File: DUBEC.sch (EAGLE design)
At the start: 69 parts

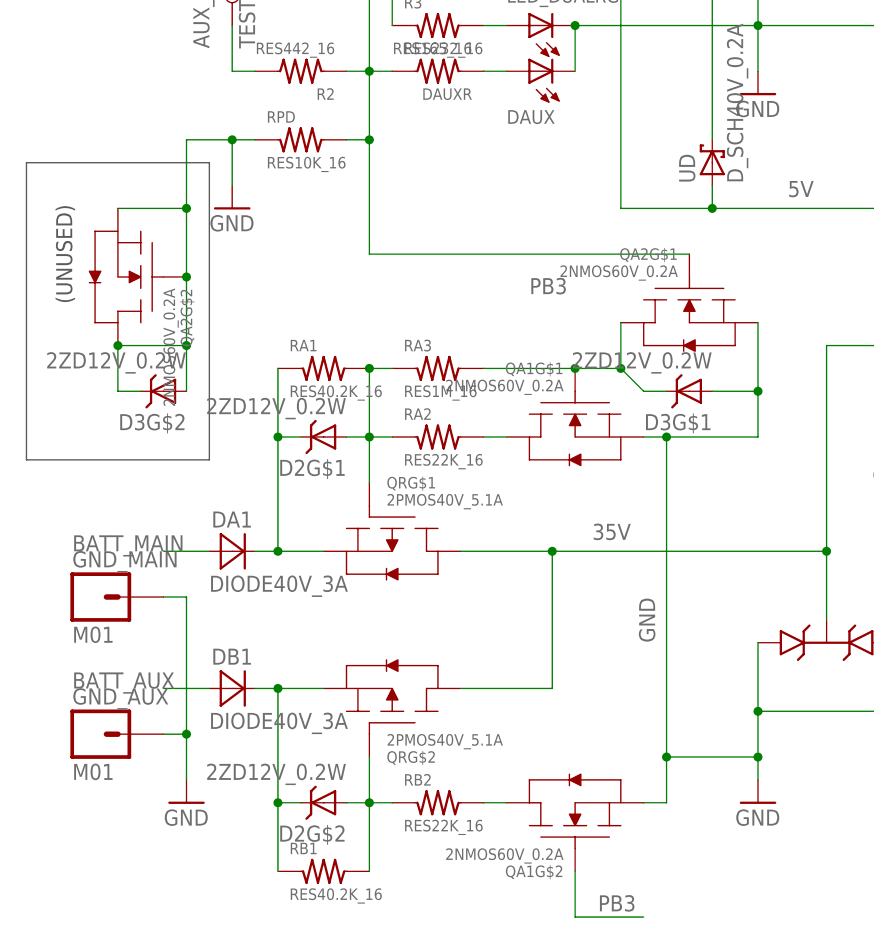
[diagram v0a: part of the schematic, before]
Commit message: Fixed one schematic error
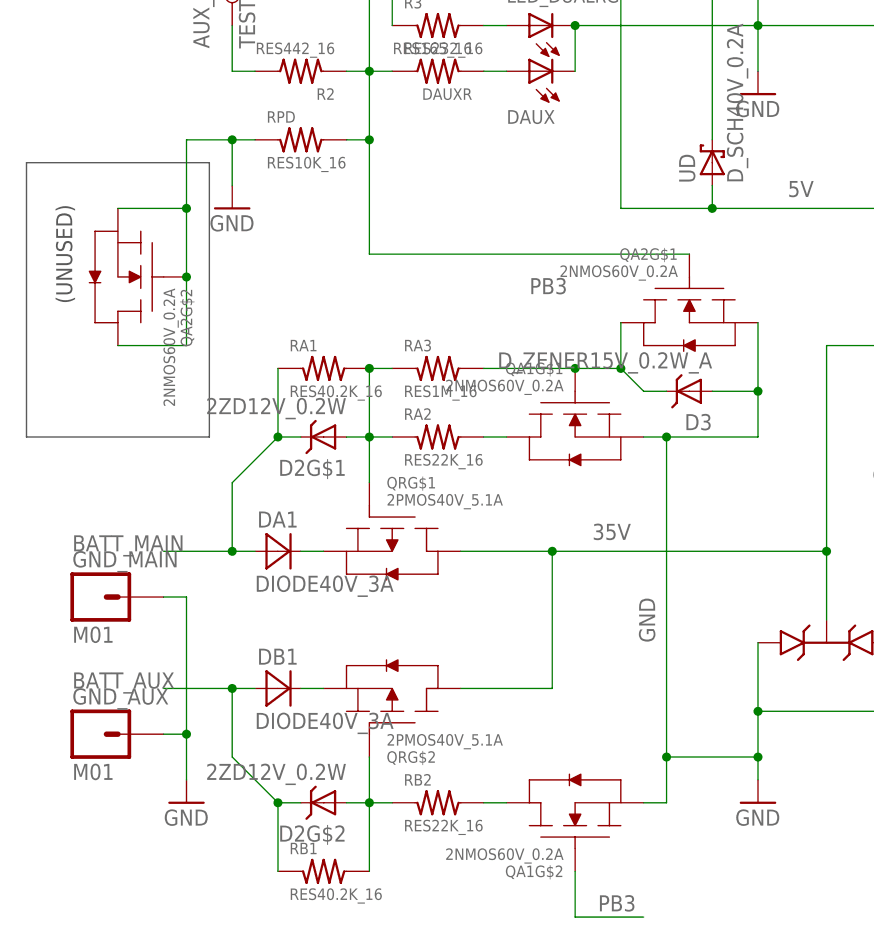
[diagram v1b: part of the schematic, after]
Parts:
- D3: value 2ZD12V_0.2W -> D_ZENER15V_0.2W_A; device dubec:2ZD12V_0.2W -> dubec:D_ZENER15V_0.2W_A
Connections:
- removed net V_AUX: D2G$2.C, DB1.C, QRG$2.S, RB1.1
- removed net V_MAIN: D2G$1.C, DA1.C, QRG$1.S, RA1.1
- new net N$6: DA1.C, QRG$1.S
- new net N$8: DB1.C, QRG$2.S
- net BATT_AUX: now also D2G$2.C, RB1.1
- net BATT_MAIN: now also D2G$1.C, RA1.1
- net GATE_MAIN_B: now also D3.C; no longer D3G$1.C
- net GND: now also D3.A; no longer D3G$1.A, D3G$2.A, D3G$2.C
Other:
- moved on the sheet: DA1, DB1
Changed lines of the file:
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@@
 <setting verticaltext="up"/>
 </settings>
-<grid distance="0.1" unitdist="inch" unit="inch" style="lines" multiple="1" display="no" altdistance="0.025" altunitdist="inch" altunit="inch"/>
+<grid distance="0.1" unitdist="inch" unit="inch" style="lines" multiple="1" display="no" altdistance="0.01" altunitdist="inch" altunit="inch"/>
 <layers>
 <layer number="1" name="Top" color="4" fill="1" visible="no" active="no"/>
@@
 <part name="RA3" library="dubec" deviceset="RES" device="1M_16" value="RES1M_16"/>
 <part name="QA2" library="dubec" deviceset="2NMOS" device="60V_0.2A"/>
-<part name="D3" library="dubec" deviceset="2ZD" device="12V_0.2W"/>
+<part name="D3" library="dubec" deviceset="D_ZENER" device="15V_0.2W_A"/>
 </parts>
 <sheets>
@@
 <text x="-129.54" y="-12.7" size="1.778" layer="97" rot="R90" align="bottom-center">(UNUSED)</text>
 <wire x1="-134.62" y1="-2.54" x2="-114.3" y2="-2.54" width="0.1524" layer="97"/>
-<wire x1="-114.3" y1="-2.54" x2="-114.3" y2="-35.56" width="0.1524" layer="97"/>
-<wire x1="-114.3" y1="-35.56" x2="-134.62" y2="-35.56" width="0.1524" layer="97"/>
-<wire x1="-134.62" y1="-35.56" x2="-134.62" y2="-2.54" width="0.1524" layer="97"/>
+<wire x1="-114.3" y1="-2.54" x2="-114.3" y2="-33.02" width="0.1524" layer="97"/>
+<wire x1="-114.3" y1="-33.02" x2="-134.62" y2="-33.02" width="0.1524" layer="97"/>
+<wire x1="-134.62" y1="-33.02" x2="-134.62" y2="-2.54" width="0.1524" layer="97"/>
 </plain>
 <instances>
@@
 <instance part="QA1" gate="G$2" x="-73.66" y="-73.66" rot="R90"/>
 <instance part="GND6" gate="1" x="-53.34" y="-73.66"/>
-<instance part="DA1" gate="G$1" x="-111.76" y="-45.72"/>
-<instance part="DB1" gate="G$1" x="-111.76" y="-60.96"/>
+<instance part="DA1" gate="G$1" x="-106.68" y="-45.72"/>
+<instance part="DB1" gate="G$1" x="-106.68" y="-60.96"/>
 <instance part="GND_MAIN" gate="G$1" x="-124.46" y="-50.8"/>
 <instance part="GND_AUX" gate="G$1" x="-124.46" y="-66.04"/>
@@
 <instance part="QA2" gate="G$2" x="-124.46" y="-15.24" rot="R180"/>
 <instance part="D3" gate="G$1" x="-60.96" y="-27.94" rot="R180"/>
-<instance part="D3" gate="G$2" x="-119.38" y="-27.94" rot="R180"/>
 </instances>
 <busses>
@@
 <wire x1="-124.46" y1="-7.62" x2="-116.84" y2="-7.62" width="0.1524" layer="91"/>
 <junction x="-116.84" y="-7.62"/>
-<pinref part="D3" gate="G$2" pin="A"/>
-<wire x1="-116.84" y1="-22.86" x2="-116.84" y2="-27.94" width="0.1524" layer="91"/>
-<junction x="-116.84" y="-22.86"/>
-<pinref part="D3" gate="G$2" pin="C"/>
-<wire x1="-121.92" y1="-27.94" x2="-124.46" y2="-27.94" width="0.1524" layer="91"/>
-<wire x1="-124.46" y1="-27.94" x2="-124.46" y2="-22.86" width="0.1524" layer="91"/>
-<junction x="-124.46" y="-22.86"/>
 </segment>
 <segment>
@@
 <wire x1="-58.42" y1="-27.94" x2="-53.34" y2="-27.94" width="0.1524" layer="91"/>
 <junction x="-53.34" y="-27.94"/>
+<label x="-64.77" y="-55.88" size="1.778" layer="95" rot="R90"/>
 <pinref part="D3" gate="G$1" pin="A"/>
-<label x="-64.77" y="-55.88" size="1.778" layer="95" rot="R90"/>
 </segment>
 </net>
@@
 <segment>
 <pinref part="DA1" gate="G$1" pin="A"/>
-<wire x1="-119.38" y1="-45.72" x2="-114.3" y2="-45.72" width="0.1524" layer="91"/>
+<wire x1="-119.38" y1="-45.72" x2="-111.76" y2="-45.72" width="0.1524" layer="91"/>
 <label x="-129.54" y="-45.72" size="1.778" layer="95"/>
-</segment>
-</net>
-<net name="V_MAIN" class="2">
-<segment>
-<pinref part="DA1" gate="G$1" pin="C"/>
-<pinref part="QR" gate="G$1" pin="S"/>
-<wire x1="-109.22" y1="-45.72" x2="-106.68" y2="-45.72" width="0.1524" layer="91"/>
+<wire x1="-111.76" y1="-45.72" x2="-109.22" y2="-45.72" width="0.1524" layer="91"/>
+<wire x1="-111.76" y1="-45.72" x2="-111.76" y2="-38.1" width="0.1524" layer="91"/>
+<junction x="-111.76" y="-45.72"/>
+<wire x1="-111.76" y1="-38.1" x2="-106.68" y2="-33.02" width="0.1524" layer="91"/>
 <pinref part="D2" gate="G$1" pin="C"/>
-<wire x1="-106.68" y1="-45.72" x2="-101.6" y2="-45.72" width="0.1524" layer="91"/>
-<wire x1="-104.14" y1="-33.02" x2="-106.68" y2="-33.02" width="0.1524" layer="91"/>
-<wire x1="-106.68" y1="-33.02" x2="-106.68" y2="-45.72" width="0.1524" layer="91"/>
-<junction x="-106.68" y="-45.72"/>
+<wire x1="-106.68" y1="-33.02" x2="-104.14" y2="-33.02" width="0.1524" layer="91"/>
 <pinref part="RA1" gate="G$1" pin="1"/>
 <wire x1="-106.68" y1="-25.4" x2="-106.68" y2="-33.02" width="0.1524" layer="91"/>
@@
 <segment>
 <pinref part="DB1" gate="G$1" pin="A"/>
-<wire x1="-119.38" y1="-60.96" x2="-114.3" y2="-60.96" width="0.1524" layer="91"/>
+<wire x1="-119.38" y1="-60.96" x2="-111.76" y2="-60.96" width="0.1524" layer="91"/>
 <label x="-129.54" y="-60.96" size="1.778" layer="95"/>
+<wire x1="-111.76" y1="-60.96" x2="-109.22" y2="-60.96" width="0.1524" layer="91"/>
+<wire x1="-111.76" y1="-60.96" x2="-111.76" y2="-68.58" width="0.1524" layer="91"/>
+<junction x="-111.76" y="-60.96"/>
+<wire x1="-111.76" y1="-68.58" x2="-106.68" y2="-73.66" width="0.1524" layer="91"/>
+<pinref part="D2" gate="G$2" pin="C"/>
+<wire x1="-106.68" y1="-73.66" x2="-104.14" y2="-73.66" width="0.1524" layer="91"/>
+<pinref part="RB1" gate="G$1" pin="1"/>
+<wire x1="-106.68" y1="-73.66" x2="-106.68" y2="-81.28" width="0.1524" layer="91"/>
+<junction x="-106.68" y="-73.66"/>
 </segment>
 <segment>
@@
 <wire x1="-33.02" y1="0" x2="-22.86" y2="0" width="0.1524" layer="91"/>
 <label x="-37.084" y="1.27" size="1.778" layer="95"/>
-</segment>
-</net>
-<net name="V_AUX" class="2">
-<segment>
-<pinref part="DB1" gate="G$1" pin="C"/>
-<pinref part="QR" gate="G$2" pin="S"/>
-<wire x1="-109.22" y1="-60.96" x2="-106.68" y2="-60.96" width="0.1524" layer="91"/>
-<pinref part="D2" gate="G$2" pin="C"/>
-<wire x1="-106.68" y1="-60.96" x2="-101.6" y2="-60.96" width="0.1524" layer="91"/>
-<wire x1="-104.14" y1="-73.66" x2="-106.68" y2="-73.66" width="0.1524" layer="91"/>
-<wire x1="-106.68" y1="-73.66" x2="-106.68" y2="-60.96" width="0.1524" layer="91"/>
-<junction x="-106.68" y="-60.96"/>
-<pinref part="RB1" gate="G$1" pin="1"/>
-<wire x1="-106.68" y1="-73.66" x2="-106.68" y2="-81.28" width="0.1524" layer="91"/>
-<junction x="-106.68" y="-73.66"/>
 </segment>
 </net>
@@
 </segment>
 </net>
+<net name="N$6" class="0">
+<segment>
+<pinref part="DA1" gate="G$1" pin="C"/>
+<pinref part="QR" gate="G$1" pin="S"/>
+<wire x1="-104.14" y1="-45.72" x2="-101.6" y2="-45.72" width="0.1524" layer="91"/>
+</segment>
+</net>
+<net name="N$8" class="0">
+<segment>
+<pinref part="DB1" gate="G$1" pin="C"/>
+<pinref part="QR" gate="G$2" pin="S"/>
+<wire x1="-104.14" y1="-60.96" x2="-101.6" y2="-60.96" width="0.1524" layer="91"/>
+</segment>
+</net>

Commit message: 1.3 ready?
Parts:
- D2: value 2ZD12V_0.2W -> 2ZD18V_0.2W; device dubec:2ZD12V_0.2W -> dubec:2ZD18V_0.2W
- QR: value 2PMOS40V_5.1A -> 2PMOS40V_8A; device dubec:2PMOS40V_5.1A -> dubec:2PMOS40V_8A
- RA1, RB1: value RES40.2K_16 -> RES10K_16; device dubec:RES40.2K_16 -> dubec:RES10K_16
- RA2, RB2: value RES22K_16 -> RES3K_16; device dubec:RES22K_16 -> dubec:RES3K_16
- RA3: value RES1M_16 -> RES200K_16; device dubec:RES1M_16 -> dubec:RES200K_16
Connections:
- net LED_X renamed LED_RED
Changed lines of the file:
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@@
 <part name="CSNUB+" library="dubec" deviceset="H1" device="0.65MM"/>
 <part name="CSNUB-" library="dubec" deviceset="H1" device="0.65MM"/>
-<part name="QR" library="dubec" deviceset="2PMOS" device="40V_5.1A"/>
-<part name="D2" library="dubec" deviceset="2ZD" device="12V_0.2W" value="2ZD12V_0.2W"/>
-<part name="RA2" library="dubec" deviceset="RES" device="22K_16" value="RES22K_16"/>
-<part name="RB2" library="dubec" deviceset="RES" device="22K_16" value="RES22K_16"/>
+<part name="QR" library="dubec" deviceset="2PMOS" device="40V_8A" value="2PMOS40V_8A"/>
+<part name="D2" library="dubec" deviceset="2ZD" device="18V_0.2W" value="2ZD18V_0.2W"/>
+<part name="RA2" library="dubec" deviceset="RES" device="3K_16" value="RES3K_16"/>
+<part name="RB2" library="dubec" deviceset="RES" device="3K_16" value="RES3K_16"/>
 <part name="QA1" library="dubec" deviceset="2NMOS" device="60V_0.2A"/>
 <part name="GND6" library="supply1" deviceset="GND" device=""/>
@@
 <part name="GND_MAIN" library="dubec" deviceset="M01" device=""/>
 <part name="GND_AUX" library="dubec" deviceset="M01" device=""/>
-<part name="RA1" library="dubec" deviceset="RES" device="40.2K_16" value="RES40.2K_16"/>
-<part name="RB1" library="dubec" deviceset="RES" device="40.2K_16" value="RES40.2K_16"/>
-<part name="RA3" library="dubec" deviceset="RES" device="1M_16" value="RES1M_16"/>
+<part name="RA1" library="dubec" deviceset="RES" device="10K_16" value="RES10K_16"/>
+<part name="RB1" library="dubec" deviceset="RES" device="10K_16" value="RES10K_16"/>
+<part name="RA3" library="dubec" deviceset="RES" device="200K_16" value="RES200K_16"/>
 <part name="QA2" library="dubec" deviceset="2NMOS" device="60V_0.2A"/>
 <part name="D3" library="dubec" deviceset="D_ZENER" device="15V_0.2W_A"/>
@@
 <wire x1="38.1" y1="58.42" x2="43.18" y2="58.42" width="0.1524" layer="91"/>
 <junction x="25.4" y="66.04"/>
-<wire x1="38.1" y1="66.04" x2="25.4" y2="66.04" width="0.1524" layer="91"/>
-<wire x1="38.1" y1="58.42" x2="38.1" y2="66.04" width="0.1524" layer="91"/>
+<wire x1="35.56" y1="66.04" x2="25.4" y2="66.04" width="0.1524" layer="91"/>
+<wire x1="38.1" y1="58.42" x2="38.1" y2="63.5" width="0.1524" layer="91"/>
+<wire x1="38.1" y1="63.5" x2="35.56" y2="66.04" width="0.1524" layer="91"/>
 <junction x="38.1" y="58.42"/>
-<wire x1="-7.62" y1="66.04" x2="12.7" y2="66.04" width="0.1524" layer="91"/>
-<label x="-5.08" y="68.58" size="1.778" layer="95"/>
-<wire x1="-7.62" y1="66.04" x2="-7.62" y2="-7.62" width="0.1524" layer="91"/>
+<wire x1="-7.62" y1="60.96" x2="-2.54" y2="66.04" width="0.1524" layer="91"/>
+<wire x1="-2.54" y1="66.04" x2="12.7" y2="66.04" width="0.1524" layer="91"/>
+<label x="-7.62" y="66.04" size="1.778" layer="95"/>
+<wire x1="-7.62" y1="60.96" x2="-7.62" y2="-7.62" width="0.1524" layer="91"/>
 <junction x="-7.62" y="-7.62"/>
 <pinref part="DTVS" gate="G$1" pin="C"/>
@@
 <wire x1="-58.42" y1="-7.62" x2="-17.78" y2="-7.62" width="0.1524" layer="91"/>
 <wire x1="-17.78" y1="-7.62" x2="-15.24" y2="-5.08" width="0.1524" layer="91"/>
-<wire x1="-15.24" y1="-5.08" x2="-15.24" y2="73.66" width="0.1524" layer="91"/>
+<wire x1="-15.24" y1="-5.08" x2="-15.24" y2="66.04" width="0.1524" layer="91"/>
 <label x="-50.038" y="-6.35" size="1.778" layer="95"/>
 <label x="66.04" y="45.72" size="1.778" layer="95"/>
@@
 <wire x1="-68.58" y1="35.56" x2="-68.58" y2="-7.62" width="0.1524" layer="91"/>
 <pinref part="5COUT2" gate="G$1" pin="1"/>
-<wire x1="-15.24" y1="73.66" x2="43.18" y2="73.66" width="0.1524" layer="91"/>
+<wire x1="-15.24" y1="66.04" x2="-7.62" y2="73.66" width="0.1524" layer="91"/>
+<wire x1="-7.62" y1="73.66" x2="43.18" y2="73.66" width="0.1524" layer="91"/>
 <wire x1="43.18" y1="73.66" x2="50.8" y2="66.04" width="0.1524" layer="91"/>
 <pinref part="5REG" gate="G$1" pin="BIAS"/>
@@
 <wire x1="68.58" y1="35.56" x2="68.58" y2="33.02" width="0.1524" layer="91"/>
 <junction x="68.58" y="35.56"/>
-<label x="-10.16" y="76.2" size="1.778" layer="95"/>
+<label x="-12.7" y="73.66" size="1.778" layer="95"/>
 </segment>
 </net>
@@
 <wire x1="-38.1" y1="-55.88" x2="-38.1" y2="-63.5" width="0.1524" layer="91"/>
 <wire x1="-38.1" y1="-63.5" x2="-53.34" y2="-63.5" width="0.1524" layer="91"/>
-<wire x1="-53.34" y1="-63.5" x2="-53.34" y2="-68.58" width="0.1524" layer="91"/>
 <junction x="-53.34" y="-63.5"/>
-<wire x1="-53.34" y1="-68.58" x2="-53.34" y2="-71.12" width="0.1524" layer="91"/>
+<wire x1="-53.34" y1="-63.5" x2="-53.34" y2="-71.12" width="0.1524" layer="91"/>
 <wire x1="-66.04" y1="-73.66" x2="-63.5" y2="-73.66" width="0.1524" layer="91"/>
-<wire x1="-63.5" y1="-73.66" x2="-63.5" y2="-68.58" width="0.1524" layer="91"/>
-<junction x="-53.34" y="-68.58"/>
-<wire x1="-63.5" y1="-68.58" x2="-53.34" y2="-68.58" width="0.1524" layer="91"/>
+<wire x1="-63.5" y1="-73.66" x2="-63.5" y2="-63.5" width="0.1524" layer="91"/>
+<junction x="-53.34" y="-63.5"/>
+<wire x1="-63.5" y1="-63.5" x2="-53.34" y2="-63.5" width="0.1524" layer="91"/>
 <wire x1="-66.04" y1="-33.02" x2="-63.5" y2="-33.02" width="0.1524" layer="91"/>
-<wire x1="-63.5" y1="-33.02" x2="-63.5" y2="-68.58" width="0.1524" layer="91"/>
-<junction x="-63.5" y="-68.58"/>
+<wire x1="-63.5" y1="-33.02" x2="-63.5" y2="-63.5" width="0.1524" layer="91"/>
+<junction x="-63.5" y="-63.5"/>
 <wire x1="-63.5" y1="-33.02" x2="-53.34" y2="-33.02" width="0.1524" layer="91"/>
 <junction x="-63.5" y="-33.02"/>
@@
 <junction x="-96.52" y="0"/>
 <wire x1="-96.52" y1="-12.7" x2="-60.96" y2="-12.7" width="0.1524" layer="91"/>
-<label x="-78.74" y="-17.145" size="1.778" layer="95"/>
+<label x="-81.28" y="-12.065" size="1.778" layer="95"/>
 <pinref part="QA2" gate="G$1" pin="G"/>
 <pinref part="DAUXR" gate="G$1" pin="2"/>
@@
 <segment>
 <pinref part="RAUXTOP" gate="G$1" pin="1"/>
-<wire x1="-33.02" y1="0" x2="-22.86" y2="0" width="0.1524" layer="91"/>
-<label x="-37.084" y="1.27" size="1.778" layer="95"/>
+<wire x1="-38.1" y1="-2.54" x2="-22.86" y2="-2.54" width="0.1524" layer="91"/>
+<wire x1="-22.86" y1="-2.54" x2="-22.86" y2="0" width="0.1524" layer="91"/>
+<label x="-37.084" y="-1.27" size="1.778" layer="95"/>
 </segment>
 </net>
@@
 </segment>
 </net>
-<net name="LED_X" class="0">
+<net name="LED_RED" class="0">
 <segment>
 <pinref part="R3" gate="G$1" pin="2"/>

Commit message: Tweaks
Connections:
- net GATE_MAIN_B: now also QA1G$2.D; no longer QA2G$1.D
- net N$10: now also QA2G$1.D; no longer QA1G$2.D
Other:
- moved on the sheet: QA1G$2, QA2G$1
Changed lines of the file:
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@@
 <instance part="RB2" gate="G$1" x="-88.9" y="-73.66"/>
 <instance part="QA1" gate="G$1" x="-73.66" y="-33.02" rot="MR270"/>
-<instance part="QA1" gate="G$2" x="-73.66" y="-73.66" rot="R90"/>
+<instance part="QA1" gate="G$2" x="-60.96" y="-20.32" rot="MR270"/>
 <instance part="GND6" gate="1" x="-53.34" y="-73.66"/>
 <instance part="DA1" gate="G$1" x="-106.68" y="-45.72"/>
@@
 <instance part="RB1" gate="G$1" x="-101.6" y="-81.28"/>
 <instance part="RA3" gate="G$1" x="-88.9" y="-25.4"/>
-<instance part="QA2" gate="G$1" x="-60.96" y="-20.32" rot="MR270"/>
+<instance part="QA2" gate="G$1" x="-73.66" y="-73.66" rot="R90"/>
 <instance part="QA2" gate="G$2" x="-124.46" y="-15.24" rot="R180"/>
 <instance part="D3" gate="G$1" x="-60.96" y="-27.94" rot="R180"/>
@@
 <segment>
 <pinref part="QA1" gate="G$1" pin="S"/>
-<pinref part="QA1" gate="G$2" pin="S"/>
 <pinref part="GND6" gate="1" pin="GND"/>
 <pinref part="DTVS" gate="G$1" pin="A1"/>
@@
 <junction x="-53.34" y="-63.5"/>
 <wire x1="-53.34" y1="-63.5" x2="-53.34" y2="-71.12" width="0.1524" layer="91"/>
-<wire x1="-66.04" y1="-73.66" x2="-63.5" y2="-73.66" width="0.1524" layer="91"/>
 <wire x1="-63.5" y1="-73.66" x2="-63.5" y2="-63.5" width="0.1524" layer="91"/>
 <junction x="-53.34" y="-63.5"/>
@@
 <junction x="-63.5" y="-33.02"/>
 <wire x1="-53.34" y1="-33.02" x2="-53.34" y2="-27.94" width="0.1524" layer="91"/>
-<pinref part="QA2" gate="G$1" pin="S"/>
-<wire x1="-53.34" y1="-27.94" x2="-53.34" y2="-20.32" width="0.1524" layer="91"/>
 <wire x1="-58.42" y1="-27.94" x2="-53.34" y2="-27.94" width="0.1524" layer="91"/>
-<junction x="-53.34" y="-27.94"/>
 <label x="-64.77" y="-55.88" size="1.778" layer="95" rot="R90"/>
 <pinref part="D3" gate="G$1" pin="A"/>
+<pinref part="QA2" gate="G$1" pin="S"/>
+<wire x1="-66.04" y1="-73.66" x2="-63.5" y2="-73.66" width="0.1524" layer="91"/>
+<pinref part="QA1" gate="G$2" pin="S"/>
+<wire x1="-53.34" y1="-20.32" x2="-53.34" y2="-27.94" width="0.1524" layer="91"/>
+<junction x="-53.34" y="-27.94"/>
 </segment>
 </net>
@@
 <wire x1="-96.52" y1="-12.7" x2="-60.96" y2="-12.7" width="0.1524" layer="91"/>
 <label x="-81.28" y="-12.065" size="1.778" layer="95"/>
-<pinref part="QA2" gate="G$1" pin="G"/>
 <pinref part="DAUXR" gate="G$1" pin="2"/>
 <wire x1="-93.98" y1="7.62" x2="-96.52" y2="7.62" width="0.1524" layer="91"/>
-</segment>
-<segment>
 <pinref part="QA1" gate="G$2" pin="G"/>
-<wire x1="-73.66" y1="-81.28" x2="-73.66" y2="-86.36" width="0.1524" layer="91"/>
+</segment>
+<segment>
 <label x="-71.12" y="-85.725" size="1.778" layer="95"/>
 <wire x1="-73.66" y1="-86.36" x2="-66.04" y2="-86.36" width="0.1524" layer="91"/>
+<pinref part="QA2" gate="G$1" pin="G"/>
+<wire x1="-73.66" y1="-81.28" x2="-73.66" y2="-86.36" width="0.1524" layer="91"/>
 </segment>
 </net>
@@
 </segment>
 </net>
-<net name="N$10" class="2">
-<segment>
-<pinref part="RB2" gate="G$1" pin="2"/>
-<pinref part="QA1" gate="G$2" pin="D"/>
-<wire x1="-83.82" y1="-73.66" x2="-81.28" y2="-73.66" width="0.1524" layer="91"/>
-</segment>
-</net>
 <net name="BATT_MAIN" class="0">
 <segment>
@@
 <pinref part="RA3" gate="G$1" pin="2"/>
 <wire x1="-73.66" y1="-25.4" x2="-68.58" y2="-25.4" width="0.1524" layer="91"/>
-<wire x1="-68.58" y1="-25.4" x2="-68.58" y2="-20.32" width="0.1524" layer="91"/>
 <junction x="-73.66" y="-25.4"/>
-<pinref part="QA2" gate="G$1" pin="D"/>
 <wire x1="-68.58" y1="-25.4" x2="-66.04" y2="-27.94" width="0.1524" layer="91"/>
-<junction x="-68.58" y="-25.4"/>
 <wire x1="-66.04" y1="-27.94" x2="-63.5" y2="-27.94" width="0.1524" layer="91"/>
 <pinref part="D3" gate="G$1" pin="C"/>
+<pinref part="QA1" gate="G$2" pin="D"/>
+<wire x1="-68.58" y1="-20.32" x2="-68.58" y2="-25.4" width="0.1524" layer="91"/>
+<junction x="-68.58" y="-25.4"/>
 </segment>
 </net>
@@
 </segment>
 </net>
+<net name="N$10" class="0">
+<segment>
+<pinref part="QA2" gate="G$1" pin="D"/>
+<pinref part="RB2" gate="G$1" pin="2"/>
+<wire x1="-81.28" y1="-73.66" x2="-83.82" y2="-73.66" width="0.1524" layer="91"/>
+</segment>
+</net>
